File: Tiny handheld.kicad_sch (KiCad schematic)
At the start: 36 parts, among them J1 Conn_01x04_Female, J2 Conn_01x04_Female, P1 USB_C_Plug_USB2.0, U1 ATtiny85-20P, U2 ATtiny85-20M, U3 EEPROM-I2CEIAJ

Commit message: designed custom 5 way button and finished up footprint assignment
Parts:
- BT1: footprint BATTCON-6.8MM -> Snapeda:BAT_BU2032-1
- C1, C2, C3, C4, C5: footprint (none) -> Capacitor_SMD:C_1206_3216Metric_Pad1.33x1.80mm_HandSolder
- D1, D2, D3: footprint (none) -> Diode_SMD:D_3220_8050Metric_Pad2.65x5.15mm_HandSolder
- J1, J2: footprint (none) -> Connector_PinHeader_2.54mm:PinHeader_1x04_P2.54mm_Vertical
- JP1, JP2, JP3, JP4: footprint (none) -> Jumper:SolderJumper-3_P1.3mm_Open_RoundedPad1.0x1.5mm_NumberLabels
- LS1: footprint (none) -> Connector_PinHeader_2.54mm:PinHeader_1x02_P2.54mm_Vertical
- P1: footprint (none) -> Snapeda:HRO_TYPE-C-31-M-12
- R1, R10, R11, R12, R2, R3, R4, R5, R6, R7, R8, R9: footprint (none) -> Resistor_SMD:R_1206_3216Metric_Pad1.30x1.75mm_HandSolder
- S1: footprint TACTILE_SWITCH_SMD_5.2MM -> (none)
- S2: footprint JOYSTICK_MINI -> Button_Switch_SMD:5 way button (joystick)
- S3: footprint JS202011SCQN -> SmacSYs:JS202011SCQN
- S4: footprint SWITCH_SP3T_SMD -> Snapeda:SW_JS202011SCQN
- U3: footprint SO08-EIAJ -> Package_SO:SOIC-8-1EP_3.9x4.9mm_P1.27mm_EP2.41x3.81mm

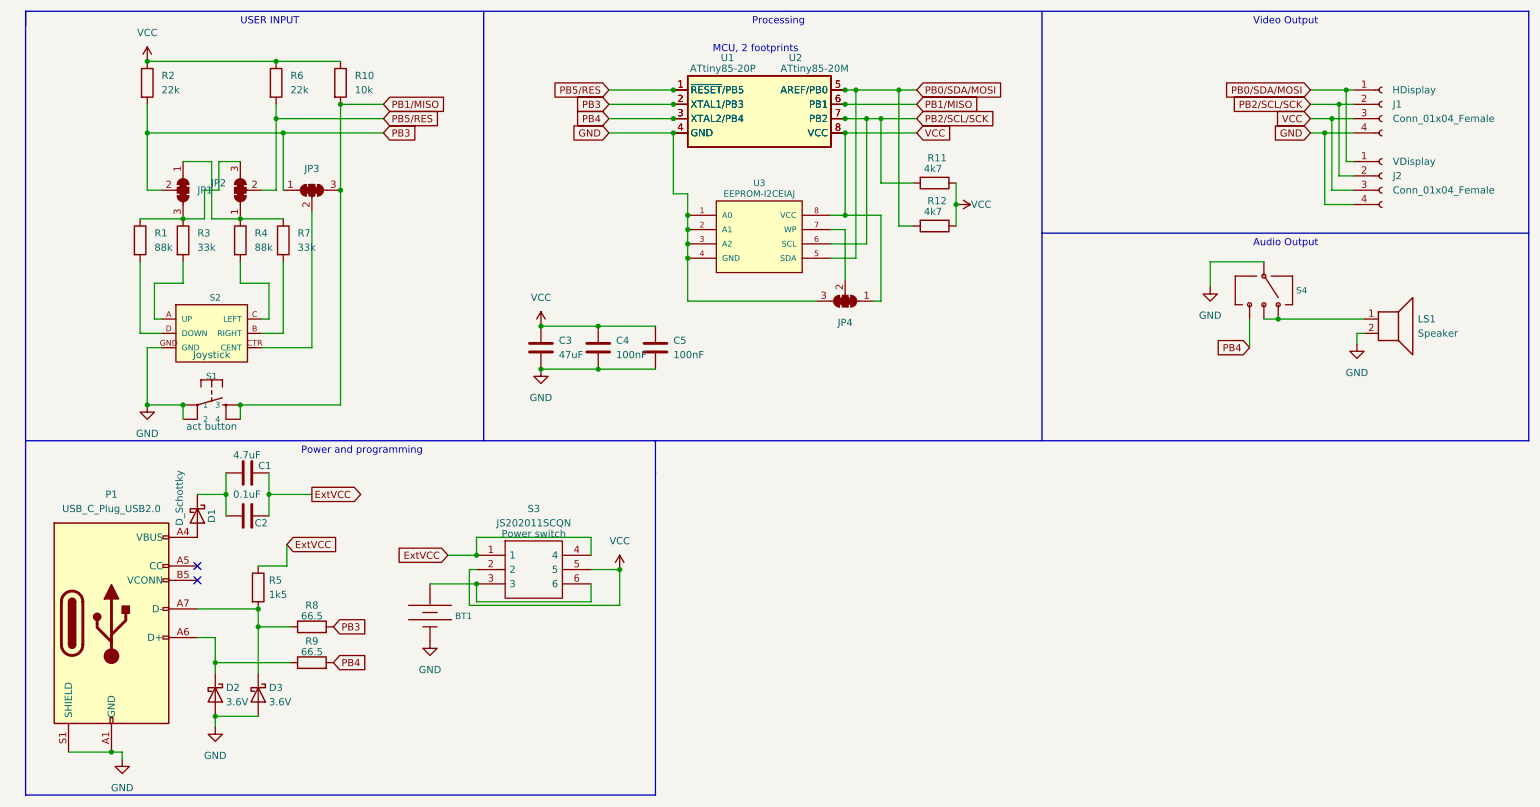
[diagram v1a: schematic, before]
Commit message: removed errors (ERC)
Left warnings in
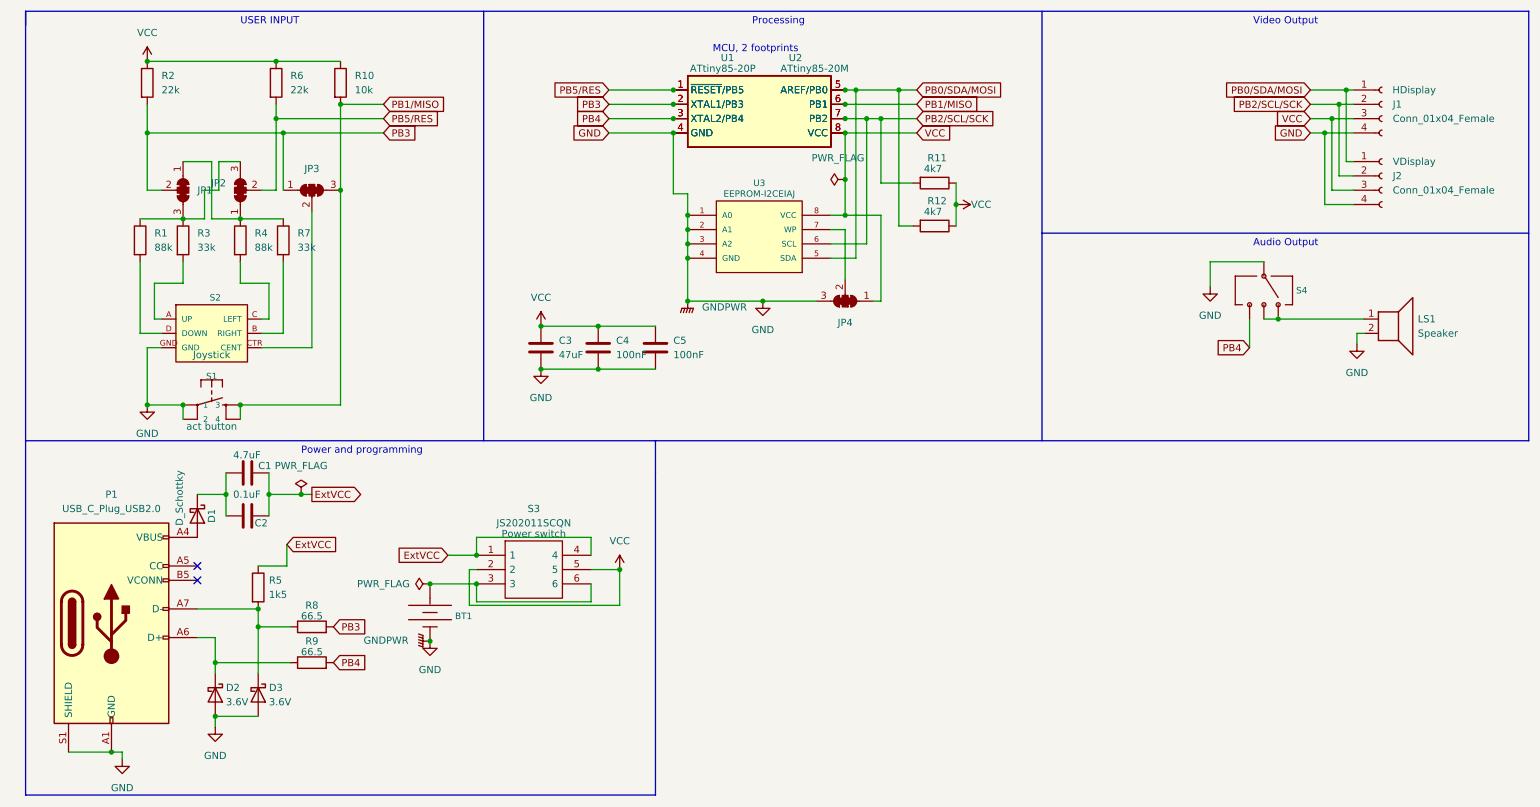
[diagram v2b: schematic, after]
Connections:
- net GND: now also U2.21 (GND)

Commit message: added missing button footprint
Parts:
- S1: footprint (none) -> Button_Switch_SMD:SW_SPST_TL3305B
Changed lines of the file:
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@@
       (effects (font (size 1.143 1.143)) hide)
     )
-    (property "Footprint" "" (id 2) (at 48.26 76.835 0)
+    (property "Footprint" "Button_Switch_SMD:SW_SPST_TL3305B" (id 2) (at 48.26 76.835 0)
       (effects (font (size 0.508 0.508)) hide)
     )
@@
     )
     (path "/ff7cddd3-0feb-4187-a60c-008a73ab2baa"
-      (reference "S1") (unit 1) (value "MOMENTARY-SWITCH-SPST-2-SMD-5.2MM") (footprint "")
+      (reference "S1") (unit 1) (value "MOMENTARY-SWITCH-SPST-2-SMD-5.2MM") (footprint "Button_Switch_SMD:SW_SPST_TL3305B")
     )
     (path "/2605f99e-3450-4ffc-961e-c01876e51427"

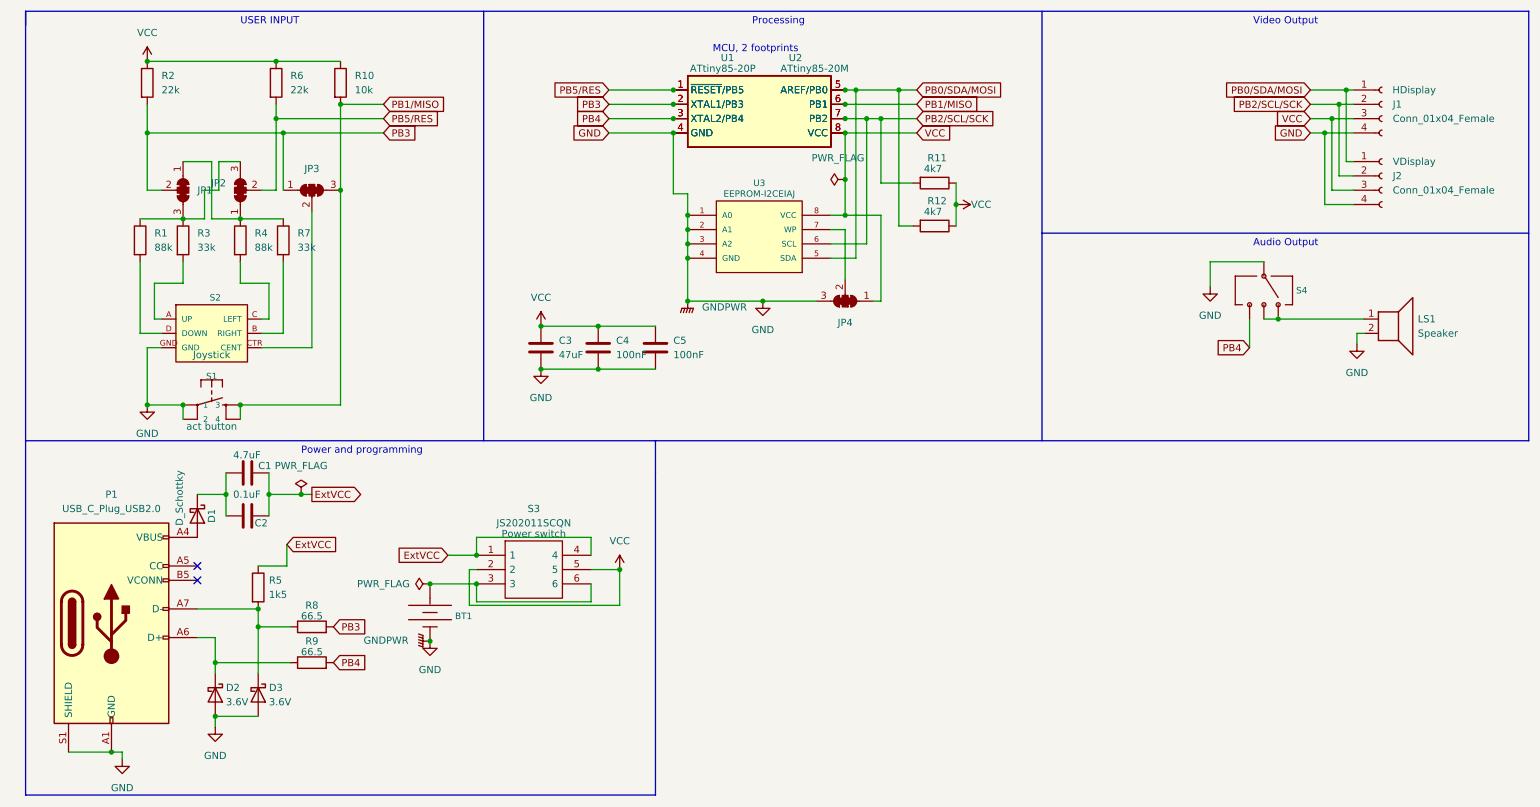
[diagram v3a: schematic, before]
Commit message: updated usb c port schematic
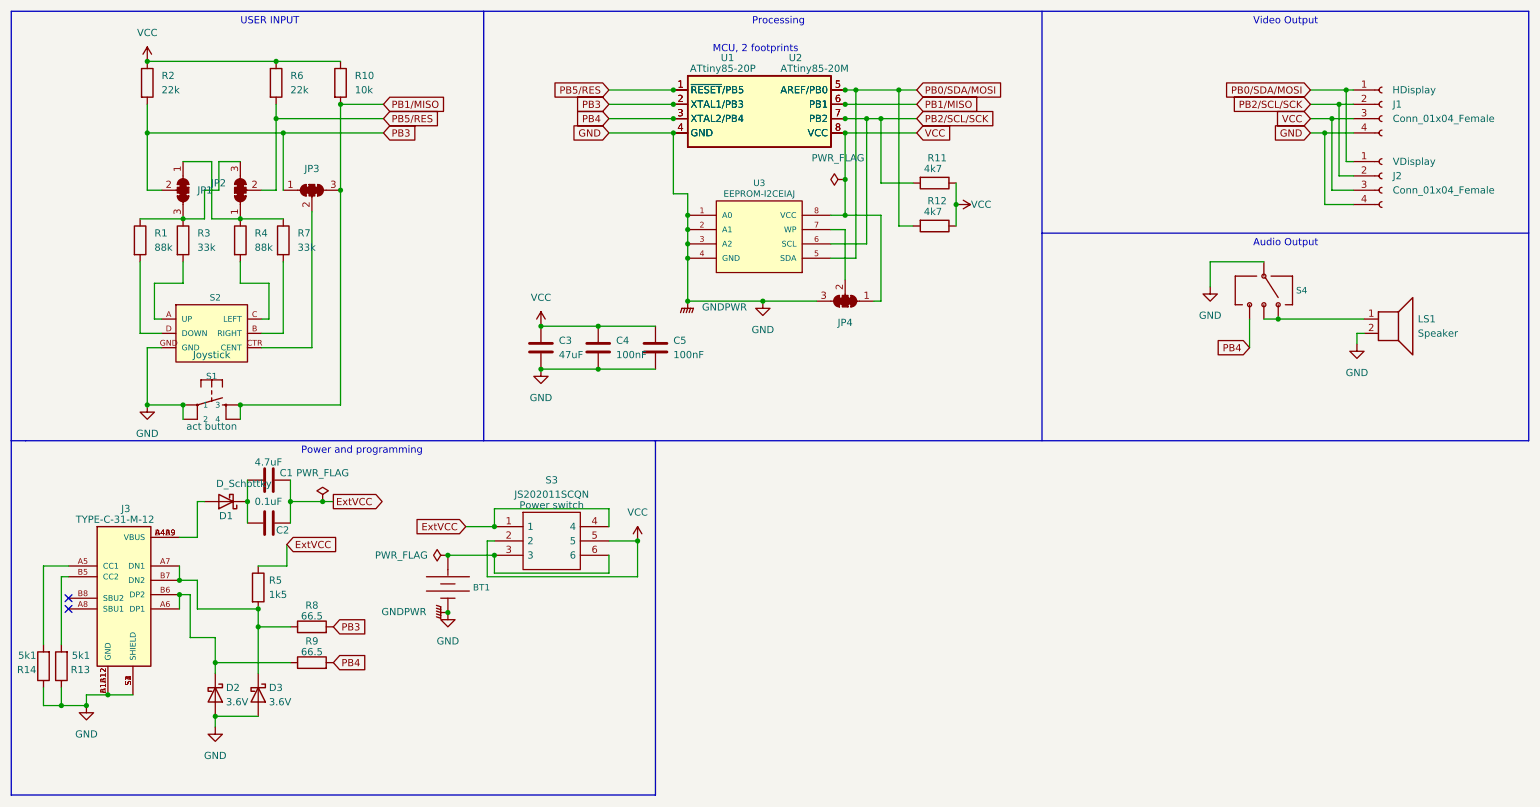
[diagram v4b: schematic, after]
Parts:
- removed P1: USB_C_Plug_USB2.0, Snapeda:HRO_TYPE-C-31-M-12, symbol Connector:USB_C_Plug_USB2.0
- added J3: TYPE-C-31-M-12, Snapeda:HRO_TYPE-C-31-M-12, symbol TYPE-C-31-M-12:TYPE-C-31-M-12
- added R13, R14: 5k1, Resistor_SMD:R_1206_3216Metric_Pad1.30x1.75mm_HandSolder, symbol Device:R
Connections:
- net GND: now also J3.A1B12 (GND), J3.B1A12 (GND), J3.S1 (SHIELD), J3.S2 (SHIELD), J3.S3 (SHIELD), J3.S4 (SHIELD), R13.1, R14.1
- net at D2.1 (K), R9.1: now also J3.A6 (DP1), J3.B6 (DP2)
- net at D3.1 (K), R5.2, R8.1: now also J3.A7 (DN1), J3.B7 (DN2)
- net at D1.2 (A): now also J3.A4B9 (VBUS), J3.B4A9 (VBUS)
- new net: J3.A5 (CC1), R14.2
- new net: J3.B5 (CC2), R13.2
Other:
- moved on the sheet: BT1, C1, C2, D1, S3

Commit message: updated footprint on attiny 85 and removed backup zip files
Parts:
- U2: footprint Package_DFN_QFN:QFN-20-1EP_4x4mm_P0.5mm_EP2.6x2.6mm -> Snapeda:QFN50P400X400X80-21N
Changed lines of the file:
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@@
   (symbol (lib_id "power:GND") (at 26.035 136.525 0) (unit 1)
     (in_bom yes) (on_board yes) (fields_autoplaced)
-    (property "Reference" "#PWR?" (id 0) (at 26.035 142.875 0)
+    (property "Reference" "#PWR0104" (id 0) (at 26.035 142.875 0)
       (effects (font (size 1.27 1.27)) hide)
     )
@@
       (effects (font (size 1.27 1.27)) (justify right))
     )
-    (property "Footprint" "Package_DFN_QFN:QFN-20-1EP_4x4mm_P0.5mm_EP2.6x2.6mm" (id 2) (at 156.21 44.45 0)
+    (property "Footprint" "Snapeda:QFN50P400X400X80-21N" (id 2) (at 156.21 44.45 0)
       (effects (font (size 1.27 1.27) italic) hide)
     )
@@
       (reference "#PWR0103") (unit 1) (value "GND") (footprint "")
     )
+    (path "/191d23e6-d60d-4ead-a16c-29496c662508"
+      (reference "#PWR0104") (unit 1) (value "GND") (footprint "")
+    )
     (path "/8f597b01-b914-42f9-803c-9063988abc27"
       (reference "#PWR0105") (unit 1) (value "VCC") (footprint "")
@@
       (reference "#PWR0114") (unit 1) (value "GNDPWR") (footprint "")
     )
-    (path "/191d23e6-d60d-4ead-a16c-29496c662508"
-      (reference "#PWR?") (unit 1) (value "GND") (footprint "")
-    )
     (path "/4b266b1c-a058-4abd-b8c0-7db2a93cb2d3"
       (reference "BT1") (unit 1) (value "BATTERY-6.8MM_SMD") (footprint "Snapeda:BAT_BU2032-1")
@@
     )
     (path "/ca613a75-40ad-4394-bb04-74b837f8bccd"
-      (reference "U2") (unit 1) (value "ATtiny85-20M") (footprint "Package_DFN_QFN:QFN-20-1EP_4x4mm_P0.5mm_EP2.6x2.6mm")
+      (reference "U2") (unit 1) (value "ATtiny85-20M") (footprint "Snapeda:QFN50P400X400X80-21N")
     )
     (path "/8508e319-db8f-4af2-9619-bd74b1def42f"

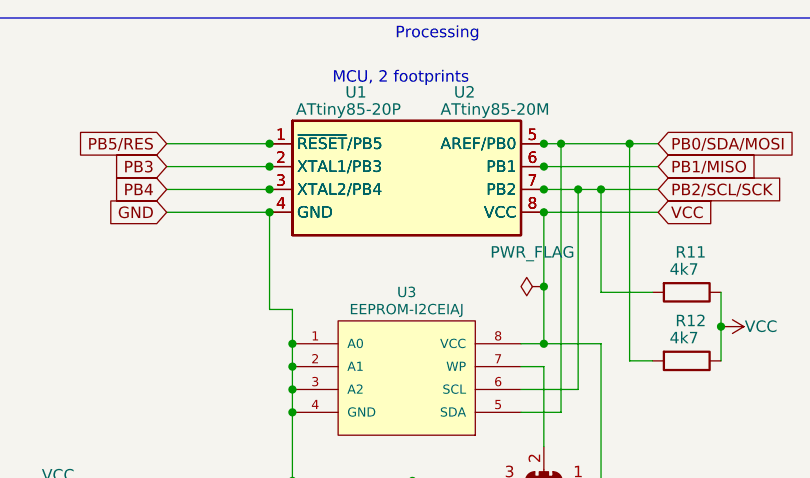
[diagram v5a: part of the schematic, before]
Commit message: fixed footprint error U2
Changed the values back to the original
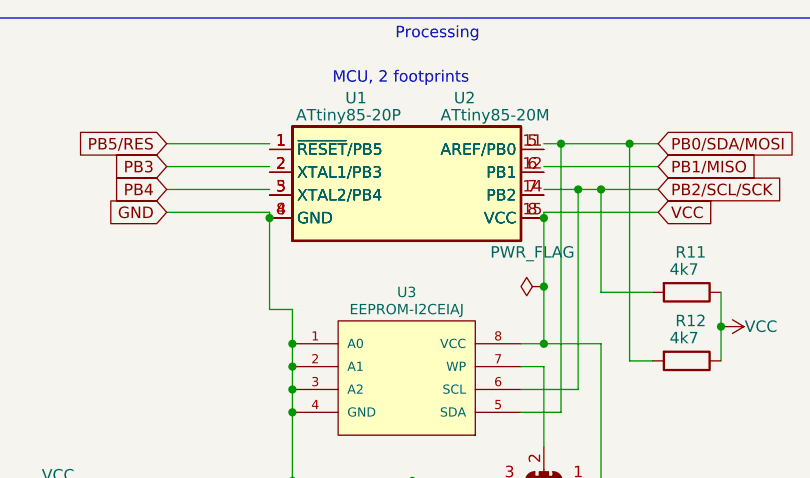
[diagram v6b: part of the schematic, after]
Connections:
- net GND: now also U2.8 (GND); no longer U2.4 (NC)
- net PB0/SDA/MOSI: no longer U1.5 (AREF/PB0), U2.5 (AREF/PB0)
- net PB1/MISO: no longer U1.6 (PB1), U2.6 (PB1)
- net PB2/SCL/SCK: no longer U1.7 (PB2), U2.7 (PB2)
- net PB3: no longer U1.2 (XTAL1/PB3), U2.2 (XTAL1/PB3)
- net PB4: no longer U1.3 (XTAL2/PB4), U2.3 (XTAL2/PB4)
- net PB5/RES: no longer U1.1 (~{RESET}/PB5), U2.1 (~{RESET}/PB5)
- net VCC: now also U2.15 (VCC); no longer U2.8 (VCC)
- new net: U1.1 (~{RESET}/PB5), U2.1 (~{RESET}/PB5)
- new net: U1.2 (XTAL1/PB3), U2.2 (XTAL1/PB3)
- new net: U1.3 (XTAL2/PB4), U2.5 (XTAL2/PB4)
- new net: U1.5 (AREF/PB0), U2.11 (AREF/PB0)
- new net: U1.6 (PB1), U2.12 (PB1)
- new net: U1.7 (PB2), U2.14 (PB2)
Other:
- moved on the sheet: U1, U2
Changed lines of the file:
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@@
   (junction (at 43.18 83.185) (diameter 0) (color 0 0 0 0)
   )
-  (junction (at 130.175 32.385) (diameter 0) (color 0 0 0 0)
-  )
   (junction (at 237.49 67.945) (diameter 0) (color 0 0 0 0)
   )
+  (junction (at 160.655 35.56) (diameter 0) (color 0 0 0 0)
+  )
   (junction (at 53.34 83.185) (diameter 0) (color 0 0 0 0)
   )
@@
   (junction (at 245.745 34.925) (diameter 0) (color 0 0 0 0)
   )
-  (junction (at 130.175 27.305) (diameter 0) (color 0 0 0 0)
-  )
   (junction (at 132.715 64.77) (diameter 0) (color 0 0 0 0)
   )
-  (junction (at 160.655 29.845) (diameter 0) (color 0 0 0 0)
+  (junction (at 130.175 35.56) (diameter 0) (color 0 0 0 0)
   )
   (junction (at 21.59 136.525) (diameter 0) (color 0 0 0 0)
@@
   (junction (at 106.68 76.835) (diameter 0) (color 0 0 0 0)
   )
-  (junction (at 160.655 27.305) (diameter 0) (color 0 0 0 0)
-  )
   (junction (at 59.69 22.225) (diameter 0) (color 0 0 0 0)
   )
@@
   (junction (at 42.545 116.84) (diameter 0) (color 0 0 0 0)
   )
-  (junction (at 160.655 34.925) (diameter 0) (color 0 0 0 0)
-  )
   (junction (at 180.34 47.625) (diameter 0) (color 0 0 0 0)
   )
@@
   (junction (at 67.945 100.33) (diameter 0) (color 0 0 0 0)
   )
-  (junction (at 130.175 29.845) (diameter 0) (color 0 0 0 0)
-  )
   (junction (at 167.005 32.385) (diameter 0) (color 0 0 0 0)
   )
   (junction (at 164.465 32.385) (diameter 0) (color 0 0 0 0)
   )
-  (junction (at 130.175 34.925) (diameter 0) (color 0 0 0 0)
-  )
   (junction (at 160.655 49.53) (diameter 0) (color 0 0 0 0)
   )
@@
   )
   (junction (at 62.23 100.33) (diameter 0) (color 0 0 0 0)
-  )
-  (junction (at 160.655 32.385) (diameter 0) (color 0 0 0 0)
   )
   (junction (at 116.84 69.215) (diameter 0) (color 0 0 0 0)
@@
     (stroke (width 0) (type default) (color 0 0 0 0))
   )
+  (wire (pts (xy 160.655 35.56) (xy 160.655 43.18))
+    (stroke (width 0) (type default) (color 0 0 0 0))
+  )
   (wire (pts (xy 250.825 45.085) (xy 247.015 45.085))
     (stroke (width 0) (type default) (color 0 0 0 0))
@@
     (stroke (width 0) (type default) (color 0 0 0 0))
   )
+  (wire (pts (xy 130.175 35.56) (xy 130.175 45.72))
+    (stroke (width 0) (type default) (color 0 0 0 0))
+  )
   (polyline (pts (xy 12.7 152.4) (xy 12.7 89.535))
     (stroke (width 0) (type default) (color 0 0 0 0))
@@
     (stroke (width 0) (type default) (color 0 0 0 0))
   )
-  (wire (pts (xy 160.655 34.925) (xy 160.655 43.18))
+  (wire (pts (xy 160.655 34.925) (xy 160.655 35.56))
     (stroke (width 0) (type default) (color 0 0 0 0))
   )
@@
     (stroke (width 0) (type default) (color 0 0 0 0))
   )
-  (wire (pts (xy 130.175 34.925) (xy 130.175 45.72))
+  (wire (pts (xy 130.175 34.925) (xy 130.175 35.56))
     (stroke (width 0) (type default) (color 0 0 0 0))
   )
@@
     (pin "2")
   )
-  (symbol (lib_id "MCU_Microchip_ATtiny:ATtiny85-20P") (at 145.415 33.655 0) (unit 1)
-    (in_bom yes) (on_board yes)
-    (property "Reference" "U1" (id 0) (at 140.97 21.59 0)
+  (symbol (lib_id "MCU_Microchip_ATtiny:ATtiny85-20P") (at 145.415 34.29 0) (unit 1)
+    (in_bom yes) (on_board yes)
+    (property "Reference" "U1" (id 0) (at 140.97 22.225 0)
       (effects (font (size 1.27 1.27)) (justify right))
     )
-    (property "Value" "ATtiny85-20P" (id 1) (at 144.78 23.495 0)
+    (property "Value" "ATtiny85-20P" (id 1) (at 144.78 24.13 0)
       (effects (font (size 1.27 1.27)) (justify right))
     )
-    (property "Footprint" "Package_DIP:DIP-8_W7.62mm" (id 2) (at 147.32 61.595 0)
+    (property "Footprint" "Package_DIP:DIP-8_W7.62mm" (id 2) (at 147.32 62.23 0)
       (effects (font (size 1.27 1.27) italic) hide)
     )
-    (property "Datasheet" "http://ww1.microchip.com/downloads/en/DeviceDoc/atmel-2586-avr-8-bit-microcontroller-attiny25-attiny45-attiny85_datasheet.pdf" (id 3) (at 160.02 57.785 0)
+    (property "Datasheet" "http://ww1.microchip.com/downloads/en/DeviceDoc/atmel-2586-avr-8-bit-microcontroller-attiny25-attiny45-attiny85_datasheet.pdf" (id 3) (at 160.02 58.42 0)
       (effects (font (size 1.27 1.27)) hide)
     )
@@
     (pin "4")
   )
-  (symbol (lib_id "MCU_Microchip_ATtiny:ATtiny85-20M") (at 145.415 41.275 0) (unit 1)
-    (in_bom yes) (on_board yes)
-    (property "Reference" "U2" (id 0) (at 153.035 21.59 0)
+  (symbol (lib_id "MCU_Microchip_ATtiny:ATtiny85-20M") (at 145.415 41.91 0) (unit 1)
+    (in_bom yes) (on_board yes)
+    (property "Reference" "U2" (id 0) (at 153.035 22.225 0)
       (effects (font (size 1.27 1.27)) (justify right))
     )
-    (property "Value" "ATtiny85-20M" (id 1) (at 161.29 23.495 0)
+    (property "Value" "ATtiny85-20M" (id 1) (at 161.29 24.13 0)
       (effects (font (size 1.27 1.27)) (justify right))
     )
-    (property "Footprint" "Snapeda:QFN50P400X400X80-21N" (id 2) (at 156.21 44.45 0)
+    (property "Footprint" "Snapeda:QFN50P400X400X80-21N" (id 2) (at 156.21 45.085 0)
       (effects (font (size 1.27 1.27) italic) hide)
     )
-    (property "Datasheet" "http://ww1.microchip.com/downloads/en/DeviceDoc/atmel-2586-avr-8-bit-microcontroller-attiny25-attiny45-attiny85_datasheet.pdf" (id 3) (at 186.055 41.91 0)
+    (property "Datasheet" "http://ww1.microchip.com/downloads/en/DeviceDoc/atmel-2586-avr-8-bit-microcontroller-attiny25-attiny45-attiny85_datasheet.pdf" (id 3) (at 186.055 42.545 0)
       (effects (font (size 1.27 1.27)) hide)
     )
     (pin "1")
     (pin "10")
+    (pin "11")
+    (pin "12")
     (pin "13")
+    (pin "14")
+    (pin "15")
     (pin "16")
     (pin "17")
@@
     (pin "21")
     (pin "3")
-    (pin "3")
-    (pin "4")
     (pin "4")
     (pin "5")
     (pin "6")
-    (pin "6")
-    (pin "7")
     (pin "7")
     (pin "8")
